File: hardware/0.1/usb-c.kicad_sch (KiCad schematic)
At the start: 30 parts, among them J100 USB_C_Receptacle, U100 TPD4EUSB30, U101 HD3SS3220, U102 TPD4EUSB30, U103 TPD4EUSB30

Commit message: continue schematic design
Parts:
- removed C103, C106: 0R, symbol Device:C
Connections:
- net USB3_TX_N: now also U101.7 (TXn)
- net USB3_TX_P: now also U101.6 (TXp)
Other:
- note removed: "May need to load 100n 0201 caps"
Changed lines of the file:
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@@
-    (stroke (width 0) (type default) (color 0 0 0 0))
-  )
-  (wire (pts (xy 224.155 94.615) (xy 222.25 94.615))
     (stroke (width 0) (type default) (color 0 0 0 0))
   )
@@
     (stroke (width 0) (type default) (color 0 0 0 0))
   )
-  (wire (pts (xy 218.44 98.425) (xy 222.25 98.425))
-    (stroke (width 0) (type default) (color 0 0 0 0))
-  )
   (wire (pts (xy 161.29 109.855) (xy 158.115 109.855))
     (stroke (width 0) (type default) (color 0 0 0 0))
@@
     (stroke (width 0) (type default) (color 0 0 0 0))
   )
-  (wire (pts (xy 210.82 93.345) (xy 207.645 93.345))
-    (stroke (width 0) (type default) (color 0 0 0 0))
-  )
   (wire (pts (xy 222.25 108.585) (xy 222.25 112.395))
     (stroke (width 0) (type default) (color 0 0 0 0))
@@
     (stroke (width 0) (type default) (color 0 0 0 0))
   )
-  (wire (pts (xy 200.66 94.615) (xy 207.645 94.615))
+  (wire (pts (xy 200.66 94.615) (xy 224.155 94.615))
     (stroke (width 0) (type default) (color 0 0 0 0))
   )
@@
     (stroke (width 0) (type default) (color 0 0 0 0))
   )
-  (wire (pts (xy 222.25 97.155) (xy 222.25 98.425))
-    (stroke (width 0) (type default) (color 0 0 0 0))
-  )
   (wire (pts (xy 38.1 121.285) (xy 38.1 133.985))
     (stroke (width 0) (type default) (color 0 0 0 0))
@@
     (stroke (width 0) (type default) (color 0 0 0 0))
   )
-  (wire (pts (xy 200.66 97.155) (xy 207.645 97.155))
+  (wire (pts (xy 200.66 97.155) (xy 224.155 97.155))
     (stroke (width 0) (type default) (color 0 0 0 0))
   )
@@
     (stroke (width 0) (type default) (color 0 0 0 0))
   )
-  (wire (pts (xy 218.44 93.345) (xy 222.25 93.345))
-    (stroke (width 0) (type default) (color 0 0 0 0))
-  )
   (wire (pts (xy 60.96 106.045) (xy 95.25 106.045))
     (stroke (width 0) (type default) (color 0 0 0 0))
@@
     (stroke (width 0) (type default) (color 0 0 0 0))
   )
-  (wire (pts (xy 222.25 94.615) (xy 222.25 93.345))
-    (stroke (width 0) (type default) (color 0 0 0 0))
-  )
-  (wire (pts (xy 207.645 97.155) (xy 207.645 98.425))
-    (stroke (width 0) (type default) (color 0 0 0 0))
-  )
   (wire (pts (xy 60.96 73.025) (xy 62.865 73.025))
     (stroke (width 0) (type default) (color 0 0 0 0))
@@
     (stroke (width 0) (type default) (color 0 0 0 0))
   )
-  (wire (pts (xy 224.155 97.155) (xy 222.25 97.155))
-    (stroke (width 0) (type default) (color 0 0 0 0))
-  )
   (wire (pts (xy 233.045 59.055) (xy 233.045 62.23))
     (stroke (width 0) (type default) (color 0 0 0 0))
@@
     (stroke (width 0) (type default) (color 0 0 0 0))
   )
-  (wire (pts (xy 207.645 94.615) (xy 207.645 93.345))
-    (stroke (width 0) (type default) (color 0 0 0 0))
-  )
   (wire (pts (xy 115.57 102.235) (xy 154.305 102.235))
     (stroke (width 0) (type default) (color 0 0 0 0))
@@
     (stroke (width 0) (type default) (color 0 0 0 0))
   )
-  (wire (pts (xy 207.645 98.425) (xy 210.82 98.425))
-    (stroke (width 0) (type default) (color 0 0 0 0))
-  )
   (polyline (pts (xy 200.66 76.835) (xy 201.93 76.835))
     (stroke (width 0) (type default) (color 0 0 0 0))
@@
   )
   (text "Don't care for \nour application" (at 203.2 81.915 0)
-    (effects (font (size 1.27 1.27)) (justify left bottom))
-  )
-  (text "May need to load \n100n 0201 caps" (at 223.52 109.22 0)
     (effects (font (size 1.27 1.27)) (justify left bottom))
   )
@@
     (pin "2")
   )
-  (symbol (lib_id "Device:C") (at 214.63 98.425 270) (mirror x) (unit 1)
-    (in_bom yes) (on_board yes)
-    (property "Reference" "C106" (id 0) (at 218.44 97.155 90))
-    (property "Value" "0R" (id 1) (at 210.82 97.155 90))
-    (property "Footprint" "" (id 2) (at 210.82 97.4598 0)
-      (effects (font (size 1.27 1.27)) hide)
-    )
-    (property "Datasheet" "~" (id 3) (at 214.63 98.425 0)
-      (effects (font (size 1.27 1.27)) hide)
-    )
-    (pin "1")
-    (pin "2")
-  )
   (symbol (lib_id "power:GND") (at 239.395 64.135 0) (unit 1)
     (in_bom yes) (on_board yes)
@@
     (pin "1")
   )
-  (symbol (lib_id "Device:C") (at 214.63 93.345 270) (mirror x) (unit 1)
-    (in_bom yes) (on_board yes)
-    (property "Reference" "C103" (id 0) (at 218.44 92.075 90))
-    (property "Value" "0R" (id 1) (at 210.82 92.075 90))
-    (property "Footprint" "" (id 2) (at 210.82 92.3798 0)
-      (effects (font (size 1.27 1.27)) hide)
-    )
-    (property "Datasheet" "~" (id 3) (at 214.63 93.345 0)
-      (effects (font (size 1.27 1.27)) hide)
-    )
-    (pin "1")
-    (pin "2")
-  )
   (symbol (lib_id "Power_Protection:TPD4EUSB30") (at 81.915 134.62 0) (unit 1)

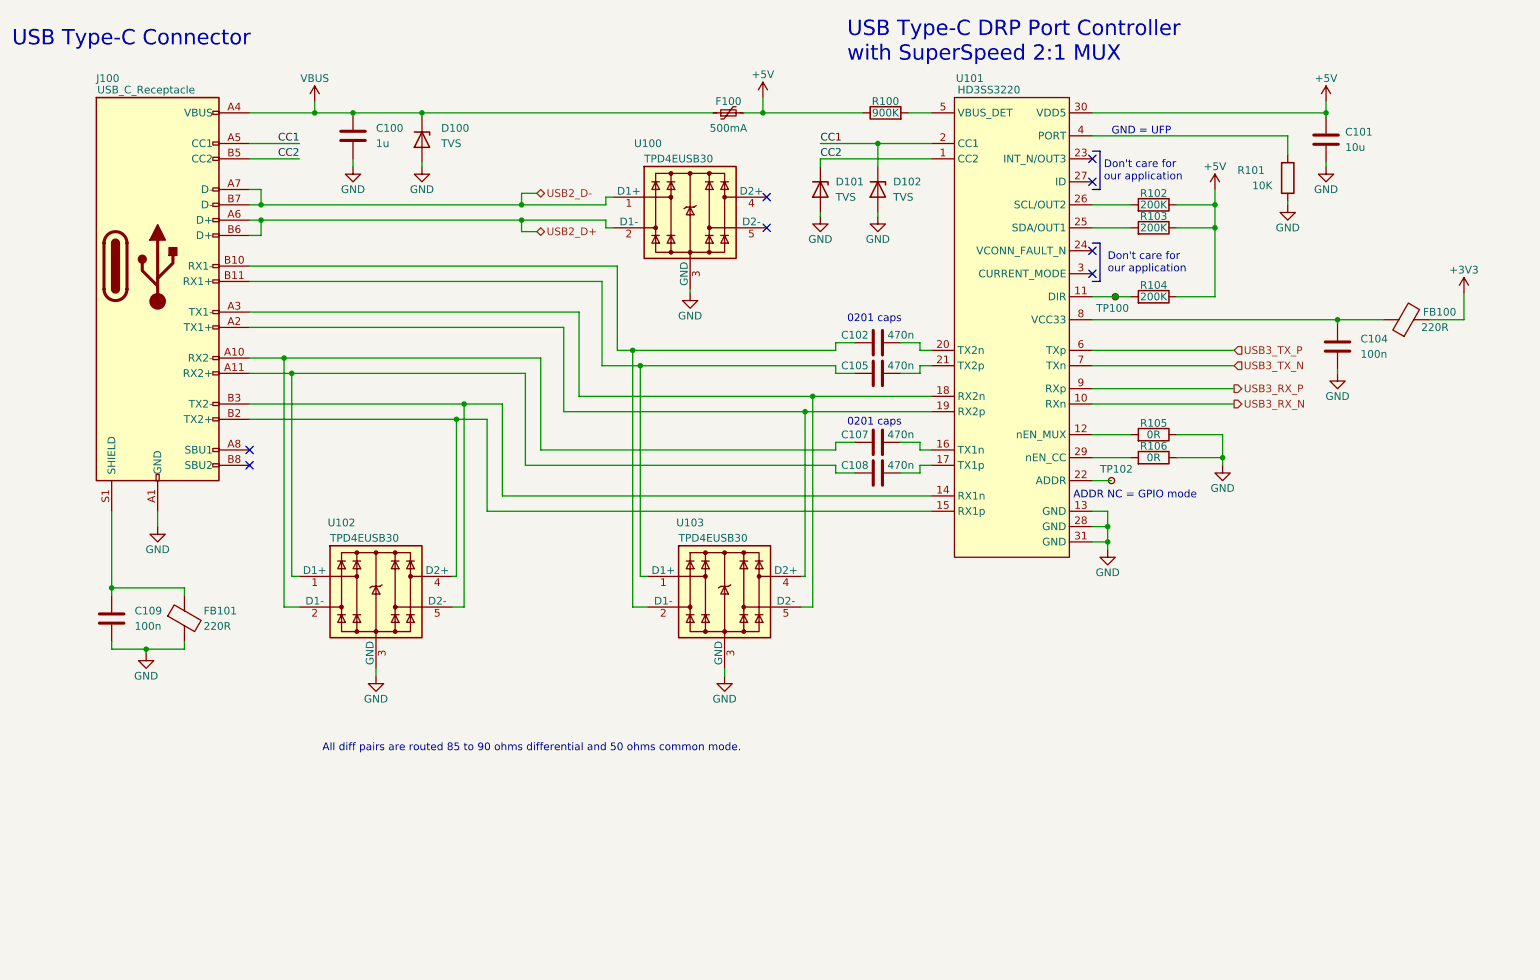
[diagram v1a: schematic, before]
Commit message: first pass schematic done
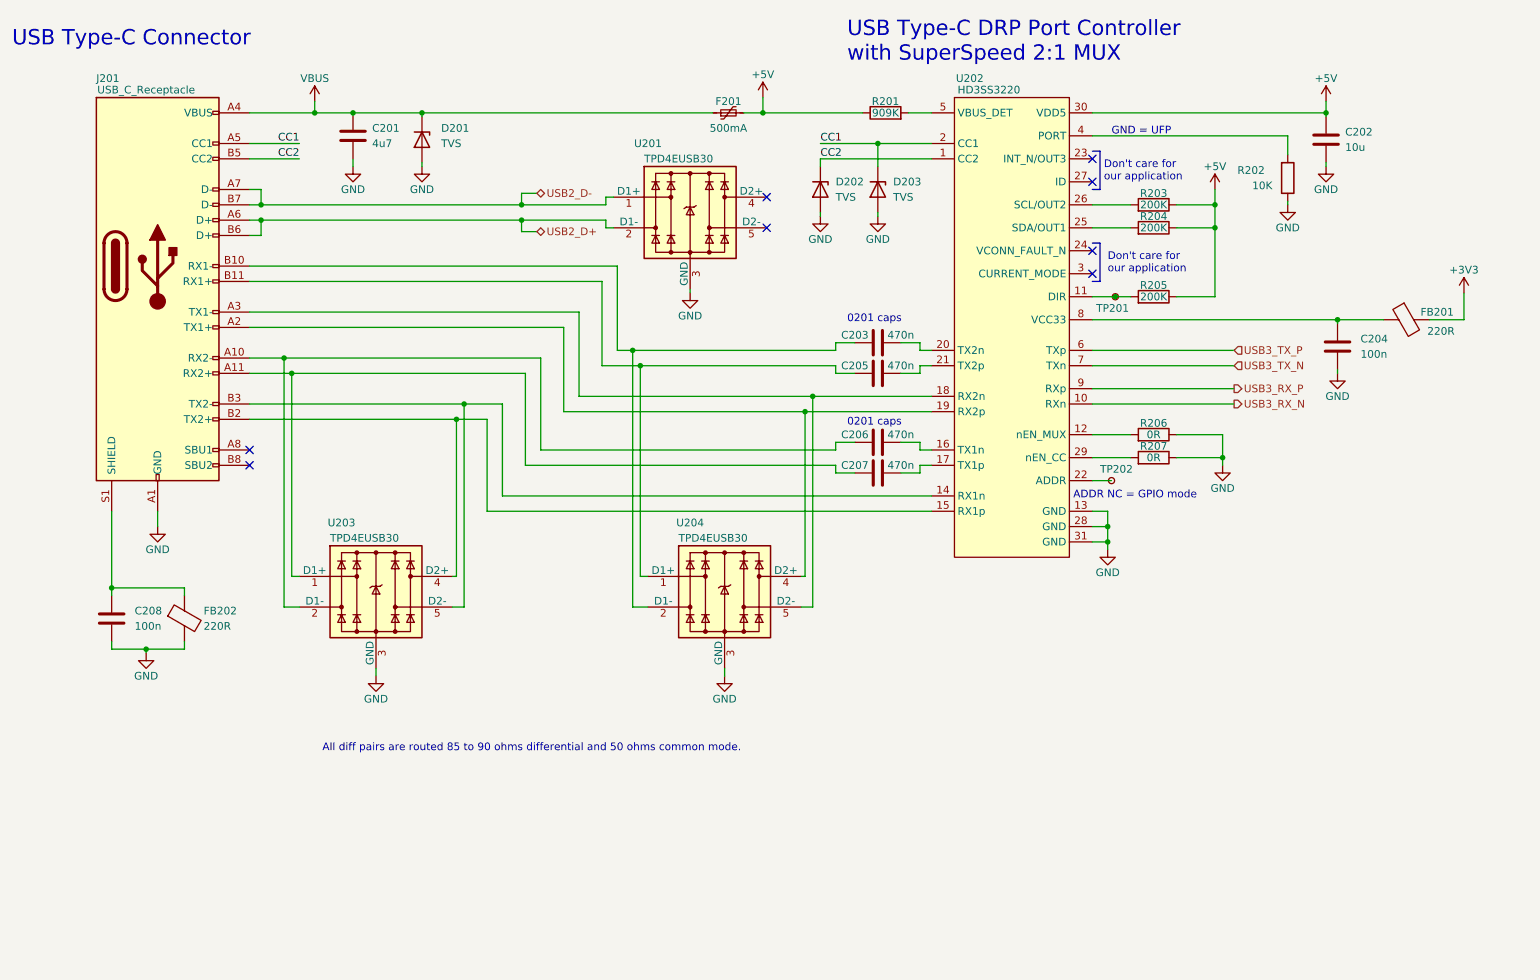
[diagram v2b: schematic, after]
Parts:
- removed FB100: 220R, symbol Device:FerriteBead
- added FB201: 220R, Resistor_SMD:R_0402_1005Metric, symbol josh-passive:Ferrite_Bead_PWR
- C201: renamed from C100; value 1u -> 4u7; footprint (none) -> Capacitor_SMD:C_0402_1005Metric; LCSC (none) -> C23733; MPN (none) -> CL05A475MP5NRNC; Manufacturer (none) -> Samsung Electro-Mechanics
- C202: renamed from C101; footprint (none) -> Capacitor_SMD:C_0603_1608Metric; LCSC (none) -> C96446; MPN (none) -> CL10A106MA8NRNC; Manufacturer (none) -> Samsung Electro-Mechanics
- C203: renamed from C102; footprint (none) -> Capacitor_SMD:C_0402_1005Metric
- C204: renamed from C104; footprint (none) -> Capacitor_SMD:C_0402_1005Metric; LCSC (none) -> C307331; MPN (none) -> CL05B104KB54PNC; Manufacturer (none) -> Samsung Electro-Mechanics
- C205: renamed from C105; footprint (none) -> Capacitor_SMD:C_0402_1005Metric
- C206: renamed from C107; footprint (none) -> Capacitor_SMD:C_0402_1005Metric
- C207: renamed from C108; footprint (none) -> Capacitor_SMD:C_0402_1005Metric
- C208: renamed from C109; footprint (none) -> Capacitor_SMD:C_0402_1005Metric; LCSC (none) -> C307331; MPN (none) -> CL05B104KB54PNC; Manufacturer (none) -> Samsung Electro-Mechanics
- F201: renamed from F100; footprint (none) -> josh-passives-smt:Fuse_0603_1608Metric; LCSC (none) -> C210357
- FB202: renamed from FB101; footprint (none) -> Resistor_SMD:R_0402_1005Metric; LCSC (none) -> C160973
- J201: renamed from J100; Digikey (none) -> 609-6109-1-ND
- R201: renamed from R100; value 900K -> 909K; footprint (none) -> Resistor_SMD:R_0402_1005Metric; LCSC (none) -> C227267; MPN (none) -> AC0402FR-07909KL; Manufacturer (none) -> Yageo
- R202: renamed from R101; footprint (none) -> Resistor_SMD:R_0402_1005Metric; LCSC (none) -> C60490; MPN (none) -> RC0402FR-0710KL; Manufacturer (none) -> Yageo
- R203: renamed from R102; footprint (none) -> Resistor_SMD:R_0402_1005Metric; LCSC (none) -> C114763; MPN (none) -> RC0402FR-07200KL; Manufacturer (none) -> Yageo
- R204: renamed from R103; footprint (none) -> Resistor_SMD:R_0402_1005Metric; LCSC (none) -> C114763; MPN (none) -> RC0402FR-07200KL; Manufacturer (none) -> Yageo
- R205: renamed from R104; footprint (none) -> Resistor_SMD:R_0402_1005Metric; LCSC (none) -> C114763; MPN (none) -> RC0402FR-07200KL; Manufacturer (none) -> Yageo
- R206: renamed from R105; footprint (none) -> Resistor_SMD:R_0402_1005Metric; LCSC (none) -> C106231; MPN (none) -> RC0402FR-070RL; Manufacturer (none) -> Yageo
- R207: renamed from R106; footprint (none) -> Resistor_SMD:R_0402_1005Metric; LCSC (none) -> C106231; MPN (none) -> RC0402FR-070RL; Manufacturer (none) -> Yageo
- TP201: renamed from TP100; value TestPoint_Small -> TP; footprint (none) -> josh-test-point:TestPoint_SMDPad_D1.0mm_NO_SILK
- TP202: renamed from TP102; value TestPoint_Small -> TP; footprint (none) -> josh-test-point:TestPoint_SMDPad_D1.0mm_NO_SILK
- U201: renamed from U100; Digikey (none) -> 296-28063-1-ND; LCSC (none) -> 296-28063-1-ND
- U202: renamed from U101; Digikey (none) -> 296-48293-1-ND
- U203: renamed from U102; Digikey (none) -> 296-28063-1-ND; LCSC (none) -> 296-28063-1-ND
- U204: renamed from U103; Digikey (none) -> 296-28063-1-ND; LCSC (none) -> 296-28063-1-ND
- renumbered D100 to D201, D101 to D202, D102 to D203
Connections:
- net +3V3: now also FB201.2
- net at C204.1, U202.8 (VCC33): now also FB201.1
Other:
- title: USB -> Voyager Logic

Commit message: finalise BOM
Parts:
- removed D202, D203: TVS, symbol Device:D_Zener
- added H201, H202, H203, H204: M2, MountingHole:MountingHole_2.2mm_M2_ISO7380_Pad, symbol Mechanical:MountingHole_Pad
- D201: value TVS -> SMF9.0CA; footprint (none) -> josh-passives-smt:D_SOD-123FL; Digikey (none) -> 18-SMF9.0CACT-ND; MPN (none) -> SMF9.0CA; Manufacturer (none) -> Littelfuse
- TP201, TP202: footprint josh-test-point:TestPoint_SMDPad_D1.0mm_NO_SILK -> josh-test-point:TestPoint_SMDPad_D0.5mm_NO_SILK
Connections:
- net +5V: now also D201.1 (K)
- net CC1: now also U201.4 (D2+)
- net CC2: now also U201.5 (D2-)
- net VBUS: no longer D201.1 (K)
- net at C208.1, FB202.1, J201.S1 (SHIELD): now also H201.1
- no-connect marks 8 -> 9
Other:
- moved on the sheet: C202, C204, D201, F201, FB201, R202, R203, R204, R205, R206, R207, TP201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
